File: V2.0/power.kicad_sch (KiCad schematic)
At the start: 10 parts, among them U5 TLV75728PDBVR

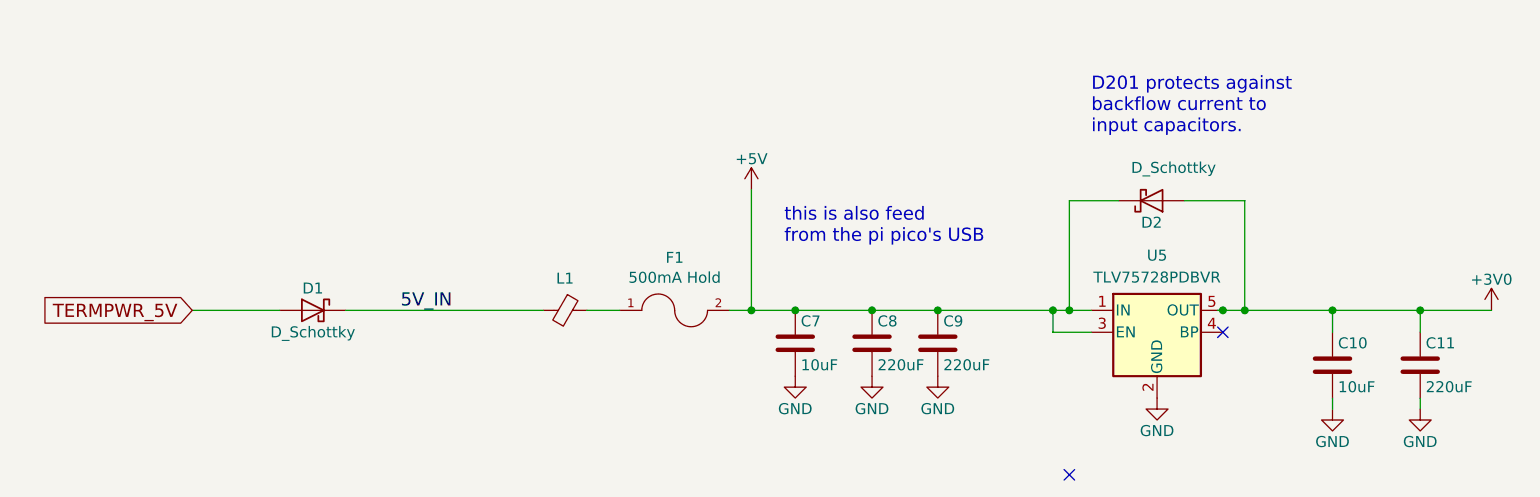
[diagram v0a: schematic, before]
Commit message: optimizations to buffers
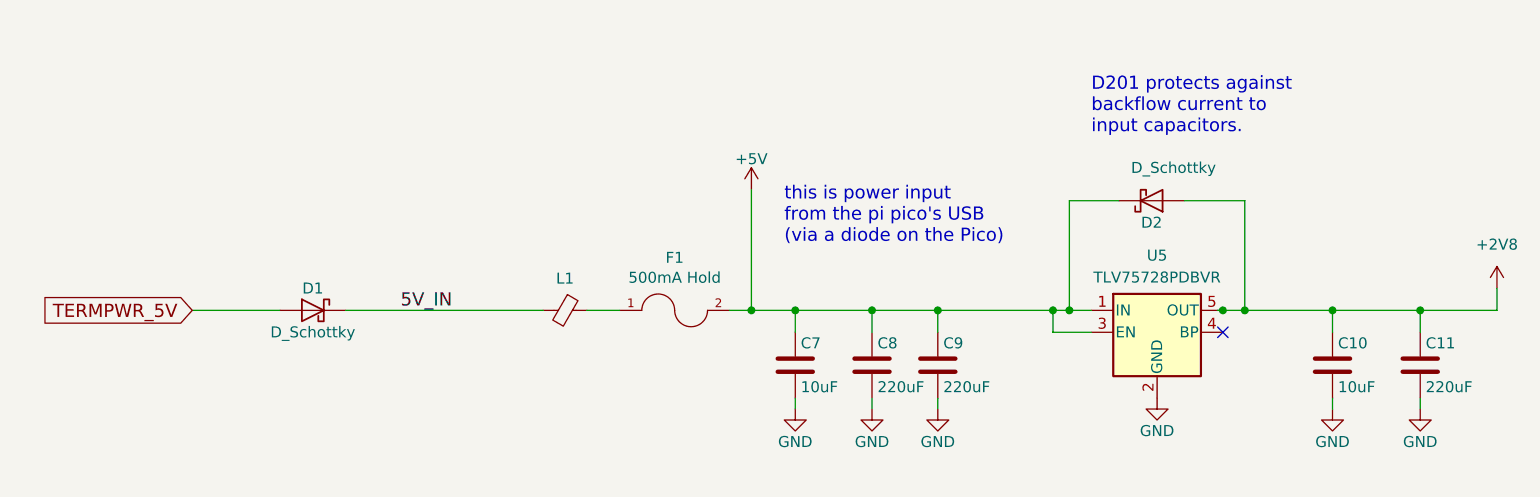
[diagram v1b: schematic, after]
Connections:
- net +3V0 renamed +2V8
- no-connect marks 2 -> 1
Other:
- note added: "this is power input from the pi pico's USB (via a diode on the Pico)"
- note removed: "this is also feed from the pi pico's USB"
- company: Derived from ZuluSCSI (TM) Pico OSHW -> ZZJ / M.D.
- title: StupidTinySCSI -> SillyTinySCSI
- moved on the sheet: C7, C8, C9

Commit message: pwr routed
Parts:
- D1, D2: footprint Diode_SMD:D_SOD-123 -> Diode_SMD:D_SOD-323; LCSC C8598 -> C191023; Manufacturer Micro Commercial Co -> (none); PartNumber MBRX120LF-TP -> (none); digikey MBRX120LF-TPMSCT-ND -> (none)
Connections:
- net +2V8: now also C9.1
- net +5V renamed 5V_REG
- net 5V_REG: no longer C9.1
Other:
- moved on the sheet: C10, C11, C9, D2, U5

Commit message: sync up
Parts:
- C11, C8, C9: LCSC C8023 -> C132272; PartNumber TAJC227K010RNJ -> TAJC227M010RNJ; digikey 478-4774-1-ND -> (none)
- L1: footprint Inductor_SMD:L_0603_1608Metric -> Inductor_SMD:L_0805_2012Metric; LCSC C1002 -> C1017; PartNumber PE-0603FB601ST -> PE-0805FB601ST; digikey 553-2384-2-ND -> (none)
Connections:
- net 5V_REG: now also L1.1; no longer F1.2
- net at F1.1: now also D1.1 (K); no longer L1.1
- net 5V_IN renamed +5VP
- net +5VP: now also F1.2; no longer D1.1 (K)
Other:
- note added: "this is power input -OR- output to the pico input: from pico's USB (via diode on pico) output: to pico if we're powered by termpower fuse is to protect the computer from us, not to protect the pico!"
- note removed: "this is power input from the pi pico's USB (via a diode on the Pico)"
- moved on the sheet: D1, F1
